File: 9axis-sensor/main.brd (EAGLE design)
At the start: 40 x 40 mm, 26 parts, among them IC1 LPC1114FDH28, IC2 MPU-9250, IC3 RN-42, IC4 MAX1555, IC5 NJM2866F33, J1 ZX62R-B-5P, J2 53261-02, SW1 SK-12D01-VG4

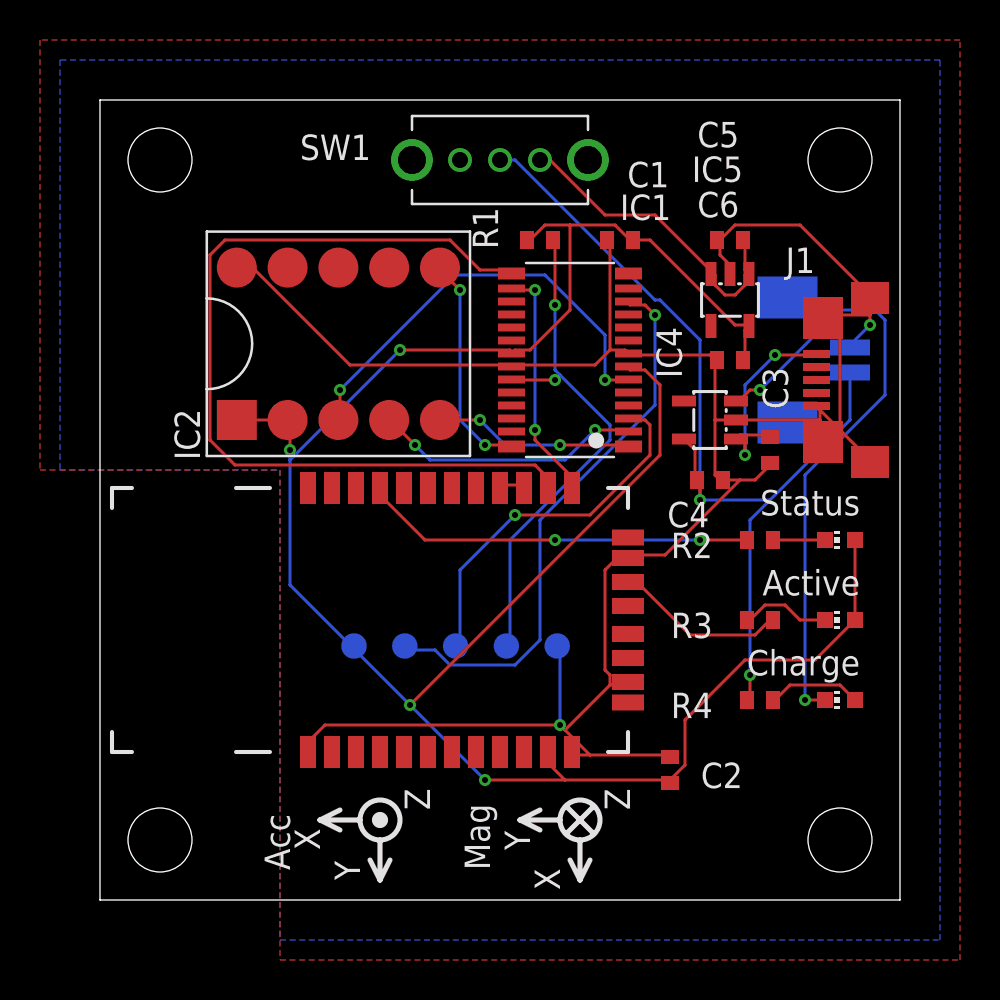
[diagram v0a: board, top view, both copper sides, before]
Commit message: バッテリ電圧測定回路を追加。基板更新。
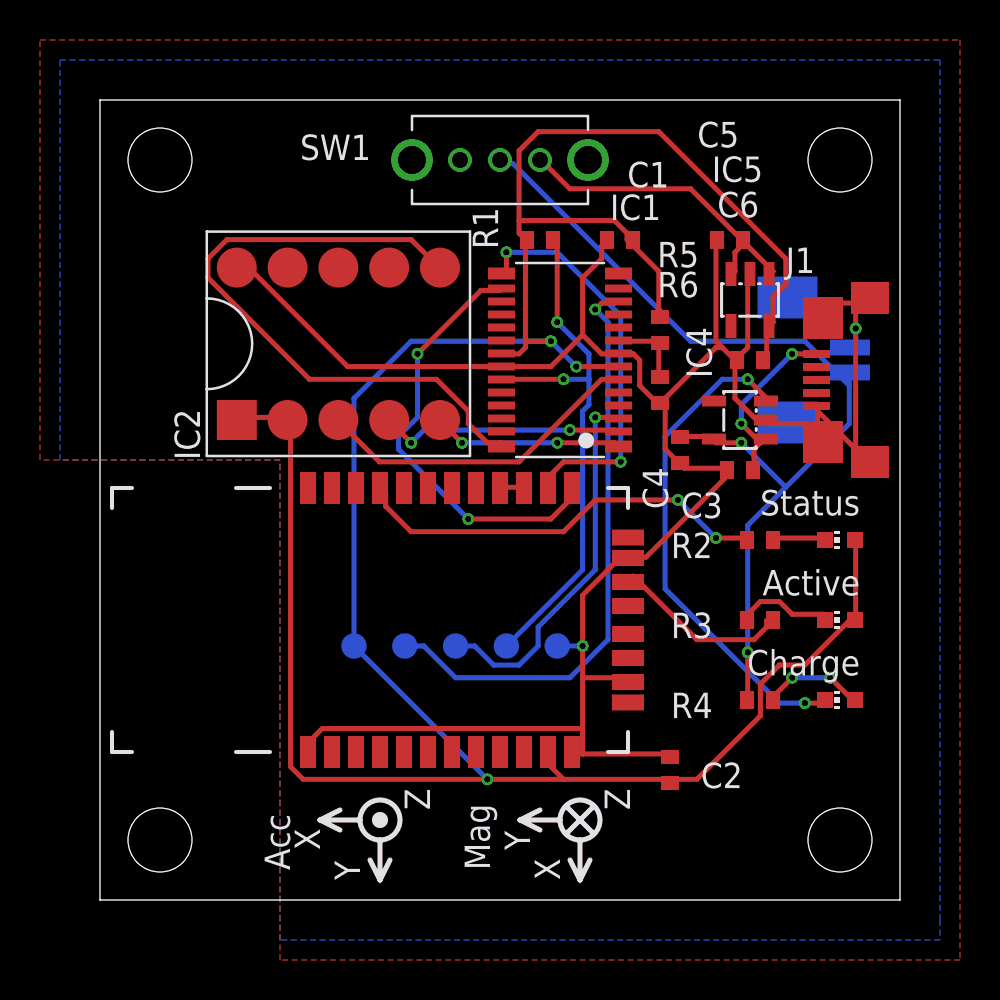
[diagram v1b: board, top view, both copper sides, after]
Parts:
- added R5, R6: 10k, rcl:R0402
- moved C4 2.12 mm to (29.0, 22.5), turned to 270 degrees
- moved C3 1.80 mm to (32.0, 21.5), turned to 180 degrees
- moved IC4 1.50 mm to (32.0, 24.0)
- moved C6 1.00 mm to (32.5, 27.0)
- moved IC5 1.00 mm to (32.5, 30.0)
- moved IC1 0.50 mm to (23.0, 27.0)
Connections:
- new net N$8: IC1.9, R5.1, R6.2
- net +3V3: now also R5.2
- net GND: now also R6.1
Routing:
- net +3V3: track 113.9 -> 140.6 mm, vias 4 -> 3
- net RX: track 43.6 -> 20.1 mm, vias 0 -> 2
- net CS: track 11.2 -> 32.1 mm, vias 2 -> 0
- net TX: track 11.8 -> 21.9 mm
- net N$5: track 31.2 -> 24.9 mm
- net SCK: track 21.9 -> 16.6 mm, vias 2 -> 0
- net N$8: track 0.00 -> 3.85 mm
- net N$2: track 11.1 -> 8.95 mm
- net SWDIO: track 28.1 -> 29.7 mm
- net STATUS: track 19.6 -> 21.1 mm
- net MOSI: track 13.4 -> 12.2 mm
- net RESET: track 26.3 -> 27.1 mm
- net ACTIVITY: track 8.68 -> 9.28 mm
- net N$6: track 4.72 -> 5.09 mm, vias 0 -> 2

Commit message: ADCの配線ミスを修正
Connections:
- net +3V3: no longer R5.2
- net BATT: now also R5.2
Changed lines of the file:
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@@
 <contactref element="IC2" pad="P$1"/>
 <contactref element="IC2" pad="P$2"/>
-<contactref element="R5" pad="2"/>
 <wire x1="27.94" y1="31.4325" x2="27.94" y2="29.21" width="0.254" layer="1"/>
 <wire x1="26.67" y1="32.7025" x2="27.94" y2="31.4325" width="0.254" layer="1"/>
-<wire x1="27.94" y1="29.21" x2="28" y2="29.15" width="0.254" layer="1"/>
 <wire x1="26.67" y1="32.7025" x2="26.65" y2="33" width="0.254" layer="1"/>
 <wire x1="33.3375" y1="28.575" x2="33.3375" y2="27.305" width="0.254" layer="1"/>
@@
 <via x="32.385" y="12.3825" extent="1-16" drill="0.3048"/>
 <via x="32.0675" y="22.86" extent="1-16" drill="0.3048"/>
+<contactref element="R5" pad="2"/>
+<wire x1="29.5275" y1="27.94" x2="28" y2="29.15" width="0" layer="19" extent="1-16"/>
 </signal>
 <signal name="N$5">

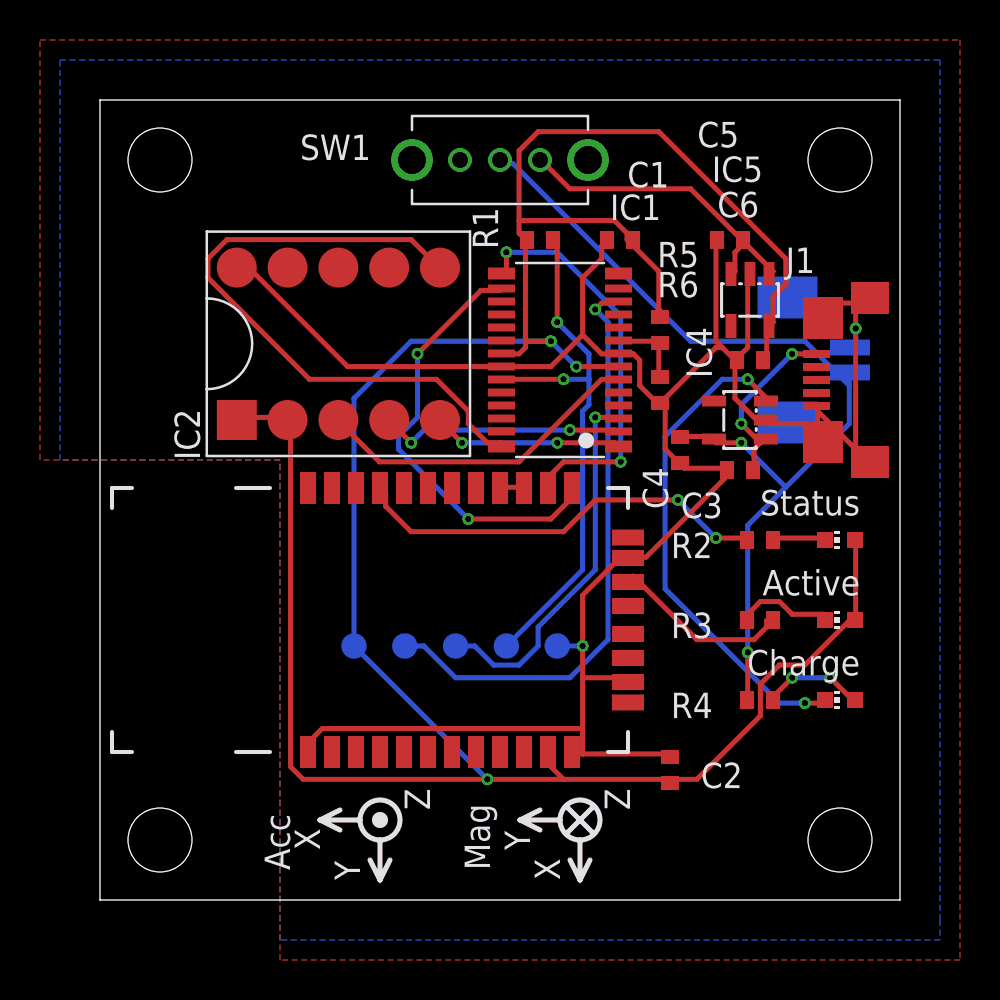
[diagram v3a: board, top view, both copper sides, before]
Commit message: チップ部品サイズを1608に変更
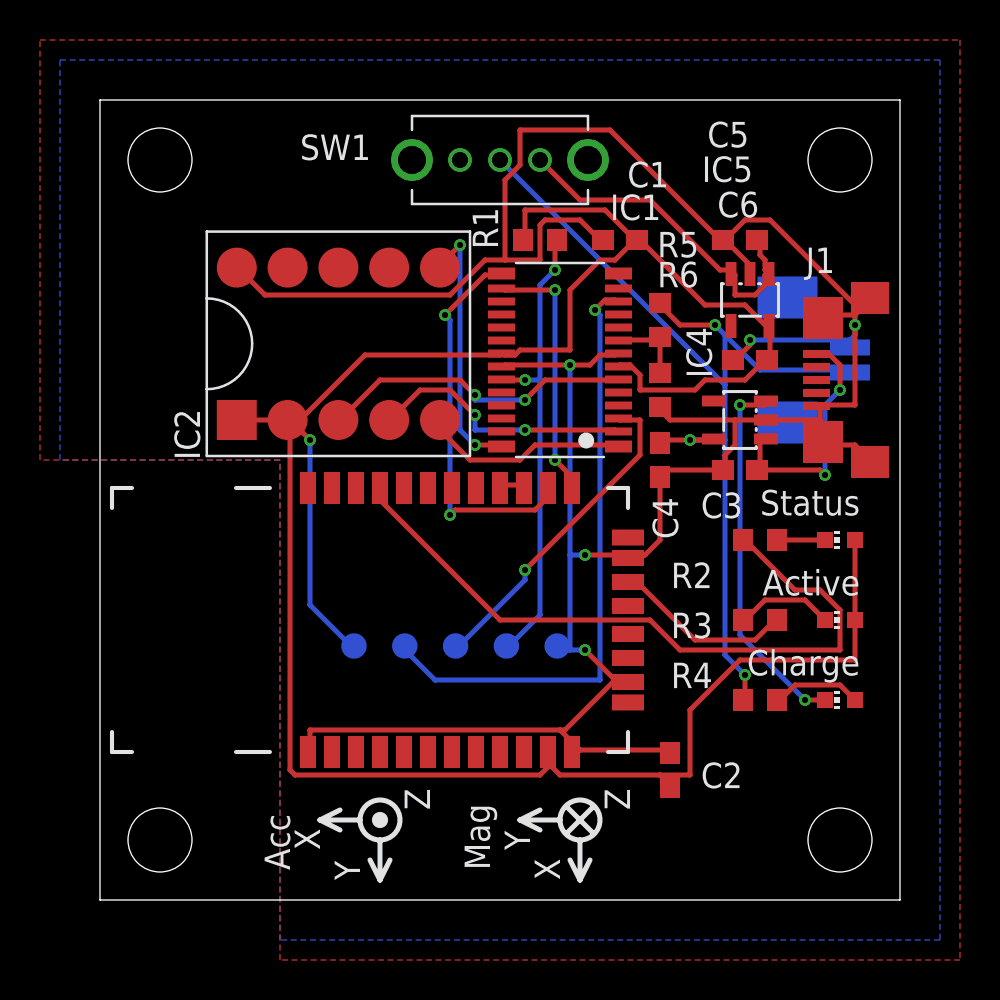
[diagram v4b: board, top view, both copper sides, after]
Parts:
- C1, C2, C5: value 1u -> 0.1u; device rcl:C0402 -> rcl:C0603
- C3, C4, C6: device rcl:C0402 -> rcl:C0603
- LED3: value Status LED -> Charge LED
- R1, R2, R3, R4, R5, R6: device rcl:R0402 -> rcl:R0603
- moved C4 1.12 mm to (28.0, 22.0)
- moved C5 0.50 mm to (32.0, 33.0)
- moved R5 0.50 mm to (28.0, 29.0)
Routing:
- net GND: track 120.3 -> 146.7 mm, vias 2 -> 5
- net CS: track 32.1 -> 13.2 mm, vias 0 -> 2
- net +3V3: track 140.5 -> 124.2 mm, vias 3 -> 1
- net STATUS: track 21.1 -> 35.0 mm, vias 2 -> 0
- net TX: track 21.9 -> 12.9 mm
- net N$5: track 24.9 -> 18.6 mm
- net RESET: track 27.1 -> 23.4 mm
- net N$2: track 8.95 -> 12.5 mm
- net BATT: track 47.1 -> 50.4 mm, vias 2 -> 3
- net SWCLK: track 18.7 -> 16.3 mm
- net N$7: track 16.2 -> 17.6 mm
- net MOSI: track 12.2 -> 13.4 mm
- net MISO: track 9.48 -> 10.4 mm, vias 2 -> 0
- net SWDIO: track 29.7 -> 30.6 mm
- net SCK: track 16.6 -> 15.8 mm, vias 0 -> 2
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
